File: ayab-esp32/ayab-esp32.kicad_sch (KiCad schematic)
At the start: 22 parts

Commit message: first draft schematic
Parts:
- gave numbers to parts that had none: 22
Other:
- sheet CONNECTORS ports: added EOL_R_LC, SPI_CIPO, SPI_COPI, SPI_CS, UART_RX, UART_TX, {SOL}; removed SOL_BUS
- sheet ESP32 ports: added EOL_R_LC, SPI_CIPO, SPI_COPI, SPI_CS, UART_RX, UART_TX, USB_VBUS, {MCU_SOL}; removed SOL_BUS
- sheet SOLENOID DRIVERS ports: added {MCU_SOL}, {SOL}; removed DRV_IN, SOL_OUT
- sheet USB ports: added USB_VBUS; removed none
- note added: "for sensing USB-serial connection"
- company: (none) -> matei
- title: (none) -> AYAB-ESP32 overview

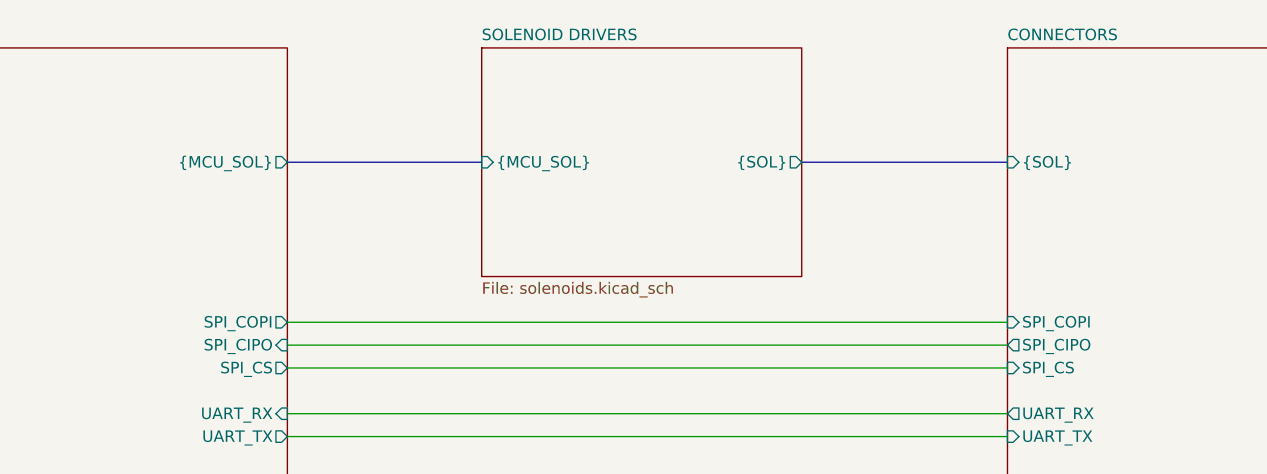
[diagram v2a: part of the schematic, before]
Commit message: add spi_sck line
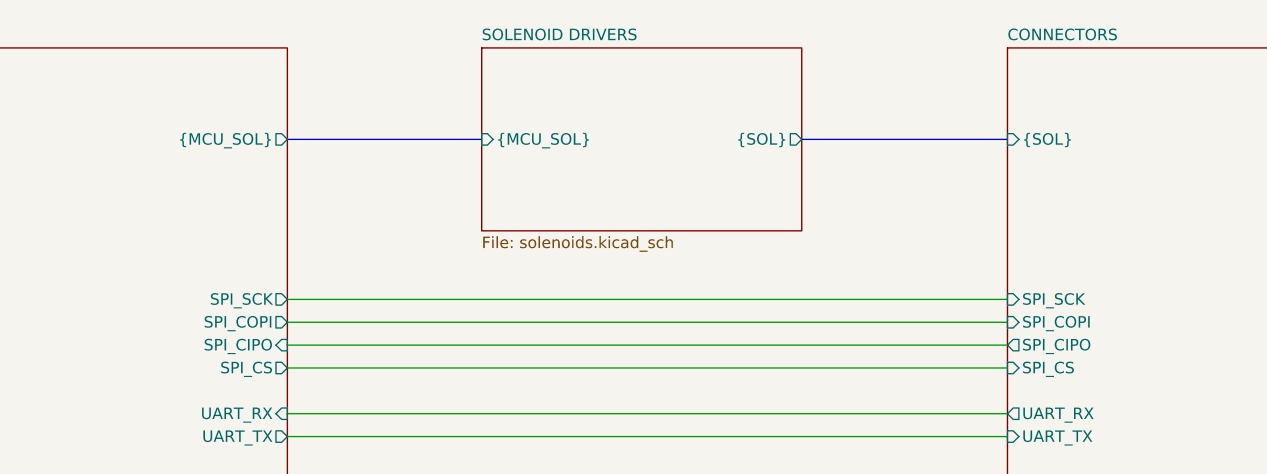
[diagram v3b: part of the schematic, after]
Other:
- sheet CONNECTORS ports: added SPI_SCK; removed none
- sheet ESP32 ports: added SPI_SCK; removed none
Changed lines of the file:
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@@
     (comment 2 "distributed under CC-BY-SA-4.0")
   )
+  (bus_alias "MCU_SOL" (members "MCU_SOL_0" "MCU_SOL_1" "MCU_SOL_2" "MCU_SOL_4" "MCU_SOL_5" "MCU_SOL_6" "MCU_SOL_7" "MCU_SOL_8" "MCU_SOL_9" "MCU_SOL_A" "MCU_SOL_B" "MCU_SOL_C" "MCU_SOL_D" "MCU_SOL_E" "MCU_SOL_F" "MCU_SOL_3"))
   (bus_alias "SOL" (members "SOL_0" "SOL_1" "SOL_2" "SOL_3" "SOL_4" "SOL_5" "SOL_6" "SOL_7" "SOL_8" "SOL_9" "SOL_A" "SOL_B" "SOL_C" "SOL_D" "SOL_E" "SOL_F"))
-  (bus_alias "MCU_SOL" (members "MCU_SOL_0" "MCU_SOL_1" "MCU_SOL_2" "MCU_SOL_4" "MCU_SOL_5" "MCU_SOL_6" "MCU_SOL_7" "MCU_SOL_8" "MCU_SOL_9" "MCU_SOL_A" "MCU_SOL_B" "MCU_SOL_C" "MCU_SOL_D" "MCU_SOL_E" "MCU_SOL_F" "MCU_SOL_3"))
   (junction (at 80.01 137.16) (diameter 0) (color 0 0 0 0)
   )
@@
     (stroke (width 0) (type default))
   )
+  (wire (pts (xy 139.7 52.07) (xy 219.71 52.07))
+    (stroke (width 0) (type default))
+  )
   (wire (pts (xy 59.69 34.29) (xy 67.31 34.29))
     (stroke (width 0) (type default))
@@
     (stroke (width 0) (type default))
   )
-  (bus (pts (xy 196.85 36.83) (xy 219.71 36.83))
+  (bus (pts (xy 196.85 34.29) (xy 219.71 34.29))
     (stroke (width 0) (type default))
   )
@@
     (stroke (width 0) (type default))
   )
-  (bus (pts (xy 139.7 36.83) (xy 161.29 36.83))
+  (bus (pts (xy 139.7 34.29) (xy 161.29 34.29))
     (stroke (width 0) (type default))
   )
@@
     )
   )
-  (sheet (at 161.29 24.13) (size 35.56 25.4) (fields_autoplaced)
+  (sheet (at 161.29 24.13) (size 35.56 20.32) (fields_autoplaced)
     (stroke (width 0.1524) (type solid))
     (fill (color 0 0 0 0.0000))
@@
       (effects (font (size 1.27 1.27)) (justify left bottom))
     )
-    (property "Sheetfile" "solenoids.kicad_sch" (at 161.29 50.1146 0)
+    (property "Sheetfile" "solenoids.kicad_sch" (at 161.29 45.0346 0)
       (effects (font (size 1.27 1.27)) (justify left top))
     )
-    (pin "{MCU_SOL}" input (at 161.29 36.83 180)
-      (effects (font (size 1.27 1.27)) (justify left))
-    )
-    (pin "{SOL}" output (at 196.85 36.83 0)
+    (pin "{MCU_SOL}" input (at 161.29 34.29 180)
+      (effects (font (size 1.27 1.27)) (justify left))
+    )
+    (pin "{SOL}" output (at 196.85 34.29 0)
       (effects (font (size 1.27 1.27)) (justify right))
     )
@@
       (effects (font (size 1.27 1.27)) (justify left top))
     )
-    (pin "{SOL}" input (at 219.71 36.83 180)
+    (pin "{SOL}" input (at 219.71 34.29 180)
       (effects (font (size 1.27 1.27)) (justify left))
     )
@@
     )
     (pin "UART_RX" output (at 219.71 64.77 180)
+      (effects (font (size 1.27 1.27)) (justify left))
+    )
+    (pin "SPI_SCK" input (at 219.71 52.07 180)
       (effects (font (size 1.27 1.27)) (justify left))
     )
@@
       (effects (font (size 1.27 1.27)) (justify left top))
     )
-    (pin "{MCU_SOL}" output (at 139.7 36.83 0)
+    (pin "{MCU_SOL}" output (at 139.7 34.29 0)
       (effects (font (size 1.27 1.27)) (justify right))
     )
@@
       (effects (font (size 1.27 1.27)) (justify left))
     )
-    (instances
+    (pin "SPI_SCK" output (at 139.7 52.07 0)
+      (effects (font (size 1.27 1.27)) (justify right))
+    )
+    (instances

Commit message: fix some comments from jpcornil-git
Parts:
- added R? (x4): 5.1k, symbol Device:R_Small_US
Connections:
- net +5V: now also R?.1, R?.1
- net CONNECTORS/ENC_BELTPHASE: now also R107.1, R108.2; no longer R103.1, R104.2
- net CONNECTORS/ENC_V1: now also R103.1, R104.2; no longer R107.1, R108.2
- net GND: now also R?.2, R?.2
- net ESP32/EOL_R_S: now reaches U101.17 (B5)
- net ESP32/EOL_R_N: now reaches U101.18 (B4)
- net CONNECTORS/EOL_R_N: now reaches U101.6 (A4)
- net CONNECTORS/EOL_R_N: now also R?.1, R?.2
- net CONNECTORS/EOL_R_S: now reaches U101.7 (A5)
- net CONNECTORS/EOL_R_S: now also R?.1, R?.2
- no-connect marks 10 -> 6
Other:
- sheet CONNECTORS ports: added EOL_R_N, EOL_R_S; removed EOL_R_LC
- sheet ESP32 ports: added EOL_R_N, EOL_R_S; removed EOL_R_LC
- moved on the sheet: C101, C102, FID101, FID102, FID103, H101, H102, H103, H104, H105, H106, H107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

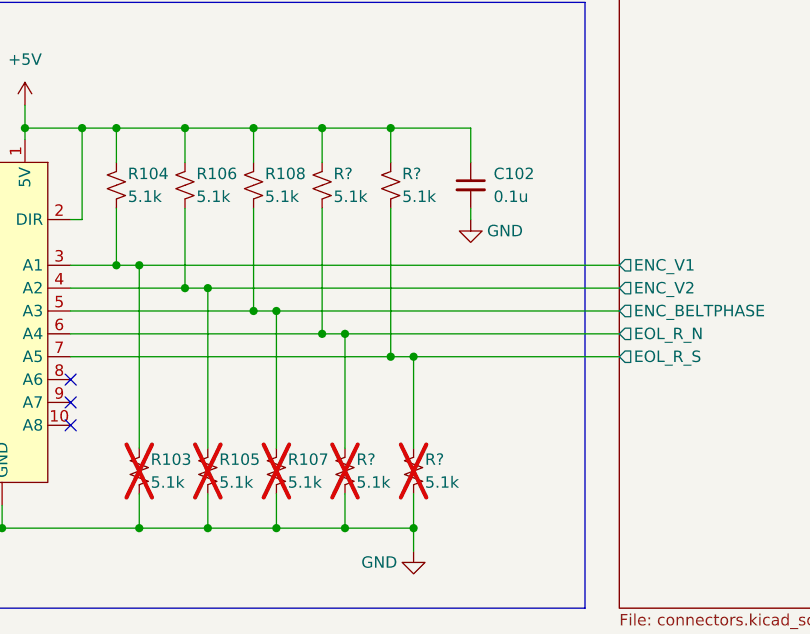
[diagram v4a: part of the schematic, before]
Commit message: add pch MOSFET for polarity protection
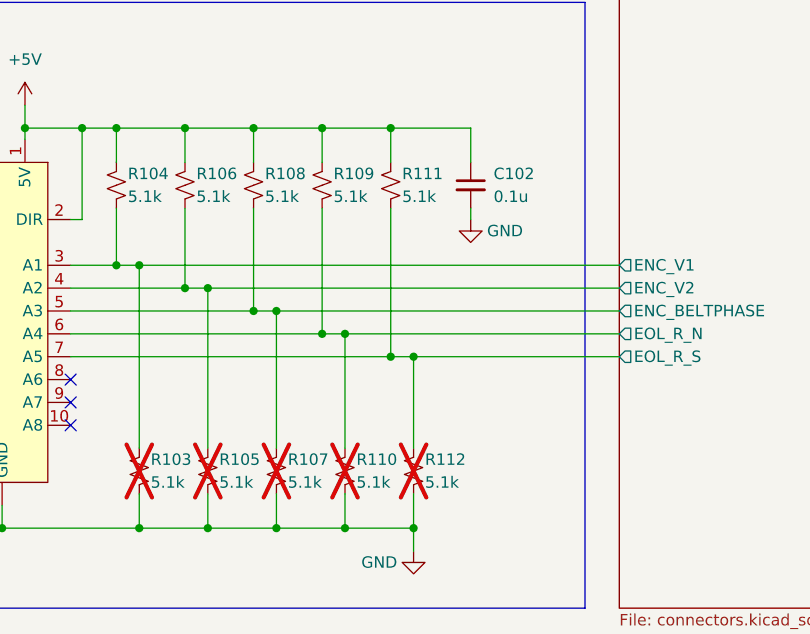
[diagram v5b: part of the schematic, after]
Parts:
- gave numbers to parts that had none: 4
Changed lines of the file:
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@@
   (symbol (lib_id "Device:R_Small_US") (at 200.66 138.43 0) (mirror y) (unit 1)
     (in_bom no) (on_board yes) (dnp yes)
-    (property "Reference" "R?" (at 201.93 137.16 0)
+    (property "Reference" "R110" (at 201.93 137.16 0)
       (effects (font (size 1.27 1.27)) (justify right))
     )
@@
       (project "ayab-esp32"
         (path "/ad16b75f-afc8-4717-a7c6-8dd7b69a18e2"
-          (reference "R?") (unit 1)
+          (reference "R110") (unit 1)
         )
       )
@@
   (symbol (lib_id "Device:R_Small_US") (at 198.12 106.68 0) (mirror y) (unit 1)
     (in_bom yes) (on_board yes) (dnp no)
-    (property "Reference" "R?" (at 199.39 105.41 0)
+    (property "Reference" "R109" (at 199.39 105.41 0)
       (effects (font (size 1.27 1.27)) (justify right))
     )
@@
       (project "ayab-esp32"
         (path "/ad16b75f-afc8-4717-a7c6-8dd7b69a18e2"
-          (reference "R?") (unit 1)
+          (reference "R109") (unit 1)
         )
       )
@@
   (symbol (lib_id "Device:R_Small_US") (at 208.28 138.43 0) (mirror y) (unit 1)
     (in_bom no) (on_board yes) (dnp yes)
-    (property "Reference" "R?" (at 209.55 137.16 0)
+    (property "Reference" "R112" (at 209.55 137.16 0)
       (effects (font (size 1.27 1.27)) (justify right))
     )
@@
       (project "ayab-esp32"
         (path "/ad16b75f-afc8-4717-a7c6-8dd7b69a18e2"
-          (reference "R?") (unit 1)
+          (reference "R112") (unit 1)
         )
       )
@@
   (symbol (lib_id "Device:R_Small_US") (at 205.74 106.68 0) (mirror y) (unit 1)
     (in_bom yes) (on_board yes) (dnp no)
-    (property "Reference" "R?" (at 207.01 105.41 0)
+    (property "Reference" "R111" (at 207.01 105.41 0)
       (effects (font (size 1.27 1.27)) (justify right))
     )
@@
       (project "ayab-esp32"
         (path "/ad16b75f-afc8-4717-a7c6-8dd7b69a18e2"
-          (reference "R?") (unit 1)
-        )
-      )
+          (reference "R111") (unit 1)
+        )
+      )

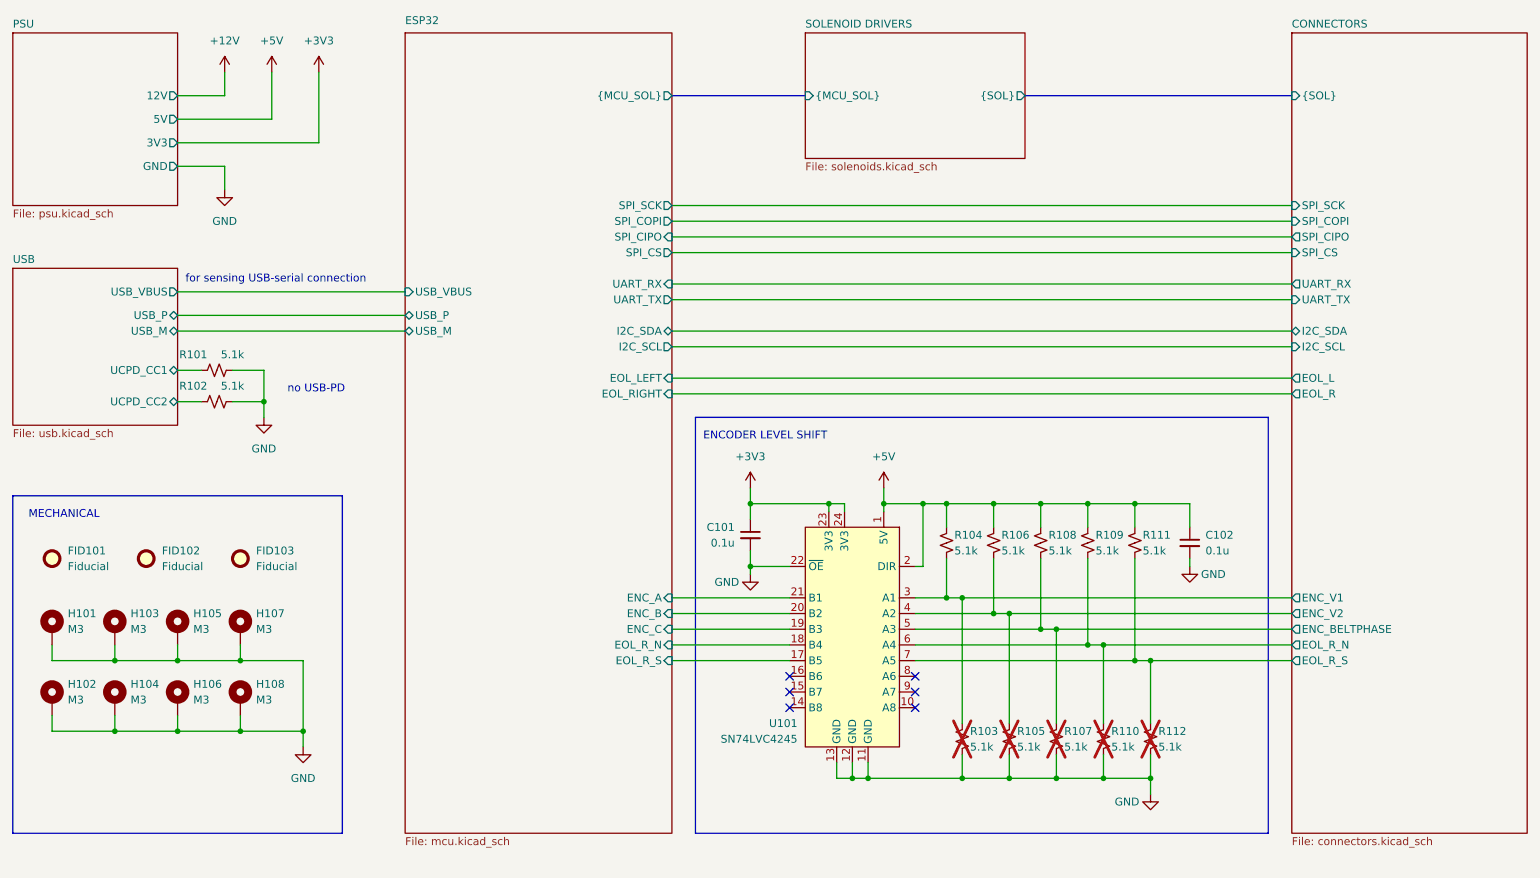
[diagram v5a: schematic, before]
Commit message: add ideal diode, remove extra uln2003a, add comparator for analog EOL sensors
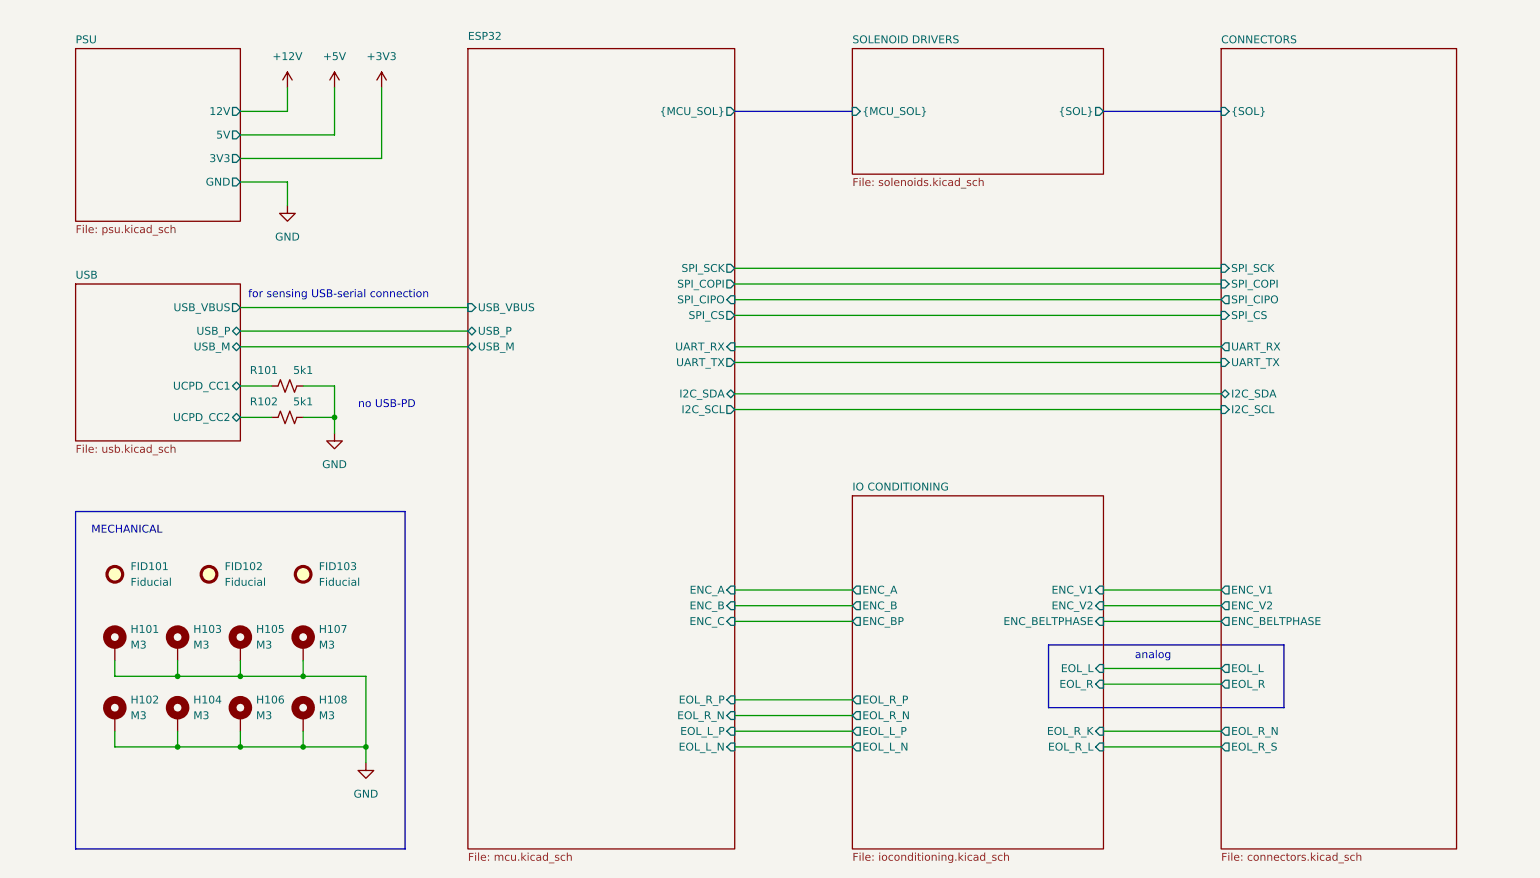
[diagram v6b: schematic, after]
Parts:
- removed C101, C102: 0.1u, symbol Device:C_Small
- removed R103, R104, R105, R106, R107, R108, R109, R110, R111, R112: 5.1k, symbol Device:R_Small_US
- removed U101: SN74LVC4245, Package_SO:TSSOP-24_4.4x6.5mm_P0.5mm, symbol matei:SN74LVC4245A
- R101, R102: value 5.1k -> 5k1
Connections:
- no-connect marks 6 -> 0
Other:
- added sheet IO CONDITIONING (ioconditioning.kicad_sch)
- sheet ESP32 ports: added EOL_L_N, EOL_L_P, EOL_R_P; removed EOL_LEFT, EOL_RIGHT, EOL_R_S
- note added: "analog"
- note removed: "ENCODER LEVEL SHIFT"
- moved on the sheet: FID101, FID102, FID103, H101, H102, H103, H104, H105, H106, H107, H108, R101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

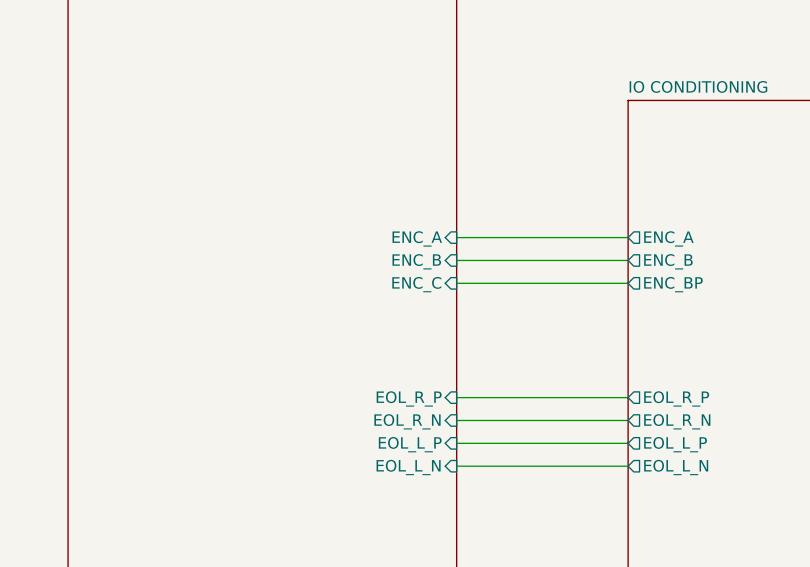
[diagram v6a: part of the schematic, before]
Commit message: fix comparator
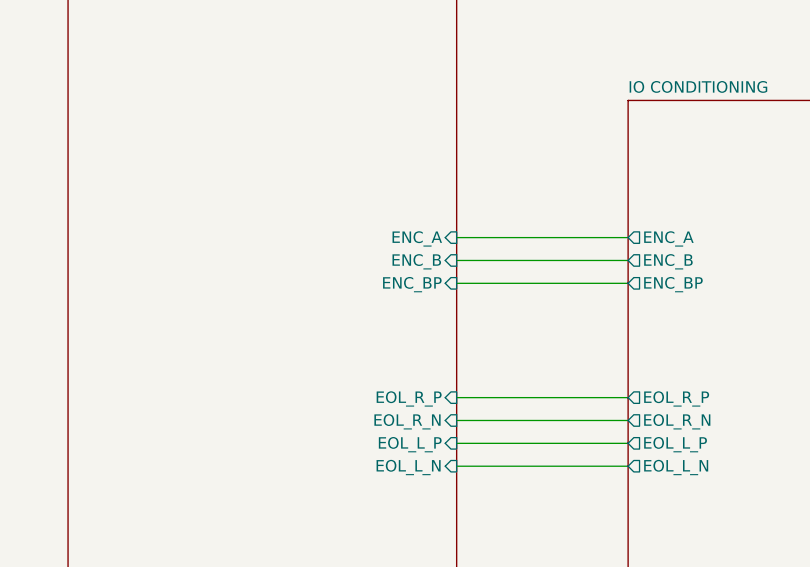
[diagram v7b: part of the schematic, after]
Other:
- sheet ESP32 ports: added ENC_BP; removed ENC_C
